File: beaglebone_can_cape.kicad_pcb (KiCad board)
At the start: 2 copper layers, 86.4 x 54.6 mm, 28 parts, among them J1 DCAN0, J2 DCAN1, J4 Conn_02x02_Top_Bottom, J5 Battery Harness, P8 BeagleBone_Black_Header, P9 BeagleBone_Black_Header, SW1 SW_Push, U1 TCAN332, U2 TCAN332, U3 LMR51430

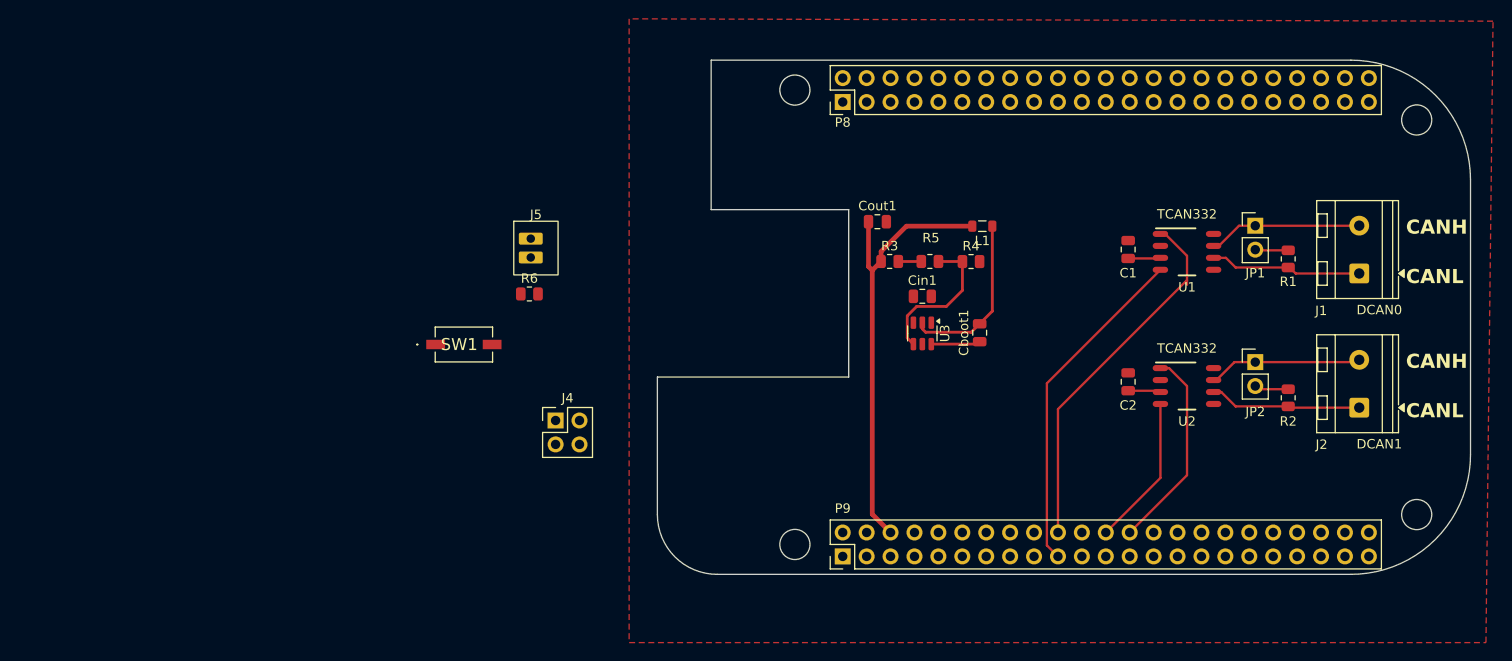
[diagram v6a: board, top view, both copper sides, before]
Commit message: PCB Version 1: Before Week 4 Meeting
* Reorganized the board to support Deutsch
* Assigned all components to have footprints
* Simplified the schematic, namely the pins
* Created the battery circuit and put on PCB

Co-Authored-By: Zach Weidner <119375087+WeidnerZ@users.noreply.github.com>
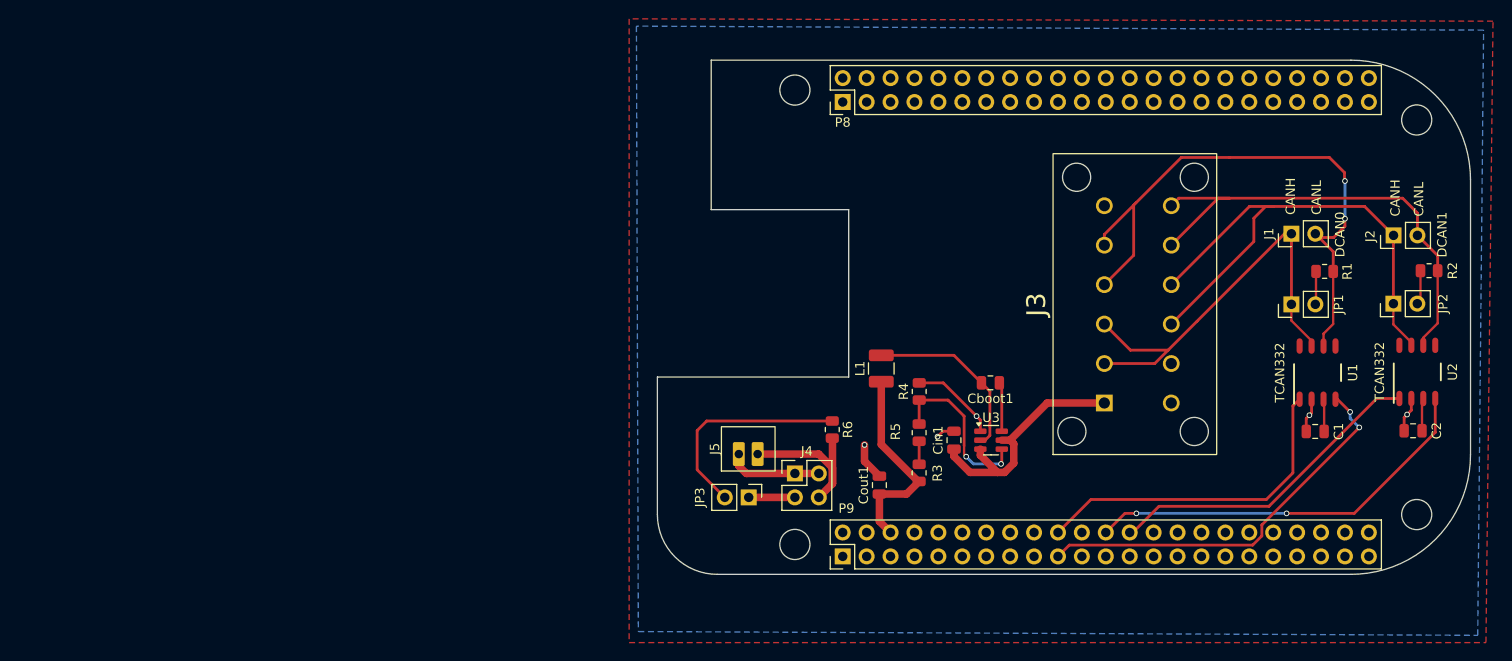
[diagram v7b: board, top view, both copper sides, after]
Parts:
- removed SW1: SW_Push, SeniorDesign:SKQYAAE010
- added J3: DTM15-12PA, Senior Design:TE_DTM15-12PA, F.Cu at (151.0, 71.3)
- added JP3: Jumper_2_Open, Connector_PinHeader_2.54mm:PinHeader_1x02_P2.54mm_Vertical, F.Cu at (109.7, 91.8)
- J1: value DCAN0 -> Conn_01x02_Pin; footprint TerminalBlock_RND:TerminalBlock_RND_205-00232_1x02_P5.08mm_Horizontal -> Connector_PinHeader_2.54mm:PinHeader_1x02_P2.54mm_Vertical
- J2: value DCAN1 -> Conn_01x02_Pin; footprint TerminalBlock_RND:TerminalBlock_RND_205-00232_1x02_P5.08mm_Horizontal -> Connector_PinHeader_2.54mm:PinHeader_1x02_P2.54mm_Vertical
- J5: footprint SeniorDesign:BatteryHolder -> Senior Design:BatteryHolder
- L1: footprint Inductor_SMD:L_0805_2012Metric -> Inductor_SMD:L_1210_3225Metric
- moved R6 35.2 mm to (118.6, 84.6), turned to -90 degrees
- moved J5 31.0 mm to (109.7, 86.7), turned to 90 degrees
- moved C2 30.7 mm to (180.3, 84.8), turned to 180 degrees
- moved Cout1 28.0 mm to (123.6, 90.5), turned to 90 degrees
- moved C1 27.7 mm to (169.9, 84.8), turned to 180 degrees
- moved J4 26.0 mm to (114.6, 89.3)
- moved U2 24.5 mm to (180.7, 78.5), turned to 90 degrees
- moved R3 22.7 mm to (127.8, 89.2), turned to 90 degrees
- moved R2 20.2 mm to (182.0, 67.8), turned to 0 degrees
- moved U1 18.9 mm to (170.1, 78.6), turned to 90 degrees
- moved J2 18.7 mm to (178.2, 64.0)
- moved L1 18.5 mm to (123.8, 78.1), turned to -90 degrees
- moved R5 18.2 mm to (127.8, 85.0), turned to 90 degrees
- moved JP2 15.9 mm to (178.2, 71.2), turned to 90 degrees
- moved Cin1 15.6 mm to (131.5, 85.8), turned to 90 degrees
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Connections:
- Cout1 pad 1: PWR -> +5V
- J1 pad 1: Net-(J1-Pin_1) -> CAN HIGH 0
- J1 pad 2: Net-(J1-Pin_2) -> CAN LOW 0
- J2 pad 1: CAN LOW 1 -> CAN HIGH 1
- J2 pad 2: CAN HIGH 1 -> CAN LOW 1
- JP1 pad 1: Net-(J1-Pin_2) -> CAN HIGH 0
- L1 pad 2: PWR -> +5V
- P8 pad 1: GNDD -> unconnected-(P8-Pin_1-Pad1)
- P8 pad 10: /GPIO68 -> unconnected-(P8-Pin_10-Pad10)
- P8 pad 11: /GPIO45 -> unconnected-(P8-Pin_11-Pad11)
- P8 pad 12: /GPIO44 -> unconnected-(P8-Pin_12-Pad12)
- P8 pad 13: /GPIO23 -> unconnected-(P8-Pin_13-Pad13)
- P8 pad 14: /GPIO26 -> unconnected-(P8-Pin_14-Pad14)
- P8 pad 15: /GPIO47 -> unconnected-(P8-Pin_15-Pad15)
- P8 pad 16: /GPIO46 -> unconnected-(P8-Pin_16-Pad16)
- P8 pad 17: /GPIO27 -> unconnected-(P8-Pin_17-Pad17)
- P8 pad 18: /GPIO65 -> unconnected-(P8-Pin_18-Pad18)
- P8 pad 19: /GPIO22 -> unconnected-(P8-Pin_19-Pad19)
- P8 pad 2: GNDD -> unconnected-(P8-Pin_2-Pad2)
- P8 pad 20: /MMC1.CMD -> unconnected-(P8-Pin_20-Pad20)
- P8 pad 21: /MMC1.CLK -> unconnected-(P8-Pin_21-Pad21)
- P8 pad 22: /MMC1.DAT5 -> unconnected-(P8-Pin_22-Pad22)
- P8 pad 23: /MMC1.DAT4 -> unconnected-(P8-Pin_23-Pad23)
- P8 pad 24: /MMC1.DAT1 -> unconnected-(P8-Pin_24-Pad24)
- P8 pad 25: /MMC1.DAT0 -> unconnected-(P8-Pin_25-Pad25)
- P8 pad 26: /LCD.PCLK -> unconnected-(P8-Pin_26-Pad26)
- P8 pad 27: /LCD.VSYNC -> unconnected-(P8-Pin_27-Pad27)
- P8 pad 28: /GPIO61 -> unconnected-(P8-Pin_28-Pad28)
- P8 pad 29: /LCD.HSYNC -> unconnected-(P8-Pin_29-Pad29)
- P8 pad 3: /MMC1.DAT6 -> unconnected-(P8-Pin_3-Pad3)
- P8 pad 30: /LCD.AC_BIAS_E -> unconnected-(P8-Pin_30-Pad30)
- P8 pad 31: /LCD.DATA14 -> unconnected-(P8-Pin_31-Pad31)
- P8 pad 32: /LCD.DATA15 -> unconnected-(P8-Pin_32-Pad32)
- P8 pad 33: /LCD.DATA13 -> unconnected-(P8-Pin_33-Pad33)
- P8 pad 34: /LCD.DATA11 -> unconnected-(P8-Pin_34-Pad34)
- P8 pad 35: /LCD.DATA12 -> unconnected-(P8-Pin_35-Pad35)
- P8 pad 36: /LCD.DATA10 -> unconnected-(P8-Pin_36-Pad36)
- P8 pad 37: /LCD.DATA8 -> unconnected-(P8-Pin_37-Pad37)
- P8 pad 38: /LCD.DATA9 -> unconnected-(P8-Pin_38-Pad38)
- P8 pad 39: /LCD.DATA6 -> unconnected-(P8-Pin_39-Pad39)
- P8 pad 4: /MMC1.DAT7 -> unconnected-(P8-Pin_4-Pad4)
- P8 pad 40: /LCD.DATA7 -> unconnected-(P8-Pin_40-Pad40)
- P8 pad 41: /LCD.DATA4 -> unconnected-(P8-Pin_41-Pad41)
- P8 pad 42: /LCD.DATA5 -> unconnected-(P8-Pin_42-Pad42)
- P8 pad 43: /LCD.DATA2 -> unconnected-(P8-Pin_43-Pad43)
- P8 pad 44: /LCD.DATA3 -> unconnected-(P8-Pin_44-Pad44)
- P8 pad 45: /LCD.DATA0 -> unconnected-(P8-Pin_45-Pad45)
- P8 pad 46: /LCD.DATA1 -> unconnected-(P8-Pin_46-Pad46)
- P8 pad 5: /MMC1.DAT2 -> unconnected-(P8-Pin_5-Pad5)
- P8 pad 6: /MMC1.DAT3 -> unconnected-(P8-Pin_6-Pad6)
- P8 pad 7: /GPIO66 -> unconnected-(P8-Pin_7-Pad7)
- P8 pad 8: /GPIO67 -> unconnected-(P8-Pin_8-Pad8)
- P8 pad 9: /GPIO69 -> unconnected-(P8-Pin_9-Pad9)
- P9 pad 1: GNDD -> unconnected-(P9-Pin_1-Pad1)
- P9 pad 10: /~{SYS_RESET} -> unconnected-(P9-Pin_10-Pad10)
- P9 pad 11: /GPIO30 -> unconnected-(P9-Pin_11-Pad11)
- P9 pad 12: /GPIO60 -> unconnected-(P9-Pin_12-Pad12)
- P9 pad 13: /GPIO31 -> unconnected-(P9-Pin_13-Pad13)
- P9 pad 14: /GPIO40 -> unconnected-(P9-Pin_14-Pad14)
- P9 pad 15: /GPIO48 -> unconnected-(P9-Pin_15-Pad15)
- P9 pad 16: /GPIO51 -> unconnected-(P9-Pin_16-Pad16)
- P9 pad 17: /GPIO4 -> unconnected-(P9-Pin_17-Pad17)
- P9 pad 18: /GPIO5 -> unconnected-(P9-Pin_18-Pad18)
- P9 pad 2: GNDD -> unconnected-(P9-Pin_2-Pad2)
- P9 pad 21: /GPIO3 -> unconnected-(P9-Pin_21-Pad21)
- P9 pad 22: /GPIO2 -> unconnected-(P9-Pin_22-Pad22)
- P9 pad 23: /GPIO49 -> unconnected-(P9-Pin_23-Pad23)
- P9 pad 25: /GPIO117 -> unconnected-(P9-Pin_25-Pad25)
- P9 pad 27: /GPIO125 -> unconnected-(P9-Pin_27-Pad27)
- P9 pad 28: /SPI1.CS0 -> unconnected-(P9-Pin_28-Pad28)
- P9 pad 29: /SPI1.D0 -> unconnected-(P9-Pin_29-Pad29)
- P9 pad 3: +3V3 -> unconnected-(P9-Pin_3-Pad3)
- P9 pad 30: /GPIO122 -> unconnected-(P9-Pin_30-Pad30)
- P9 pad 31: /SPI1.SCLK -> unconnected-(P9-Pin_31-Pad31)
- P9 pad 32: +1V8 -> unconnected-(P9-Pin_32-Pad32)
- P9 pad 33: /AIN4 -> unconnected-(P9-Pin_33-Pad33)
- P9 pad 34: GNDA -> unconnected-(P9-Pin_34-Pad34)
- P9 pad 35: /AIN6 -> unconnected-(P9-Pin_35-Pad35)
- P9 pad 36: /AIN5 -> unconnected-(P9-Pin_36-Pad36)
- P9 pad 37: /AIN2 -> unconnected-(P9-Pin_37-Pad37)
- P9 pad 38: /AIN3 -> unconnected-(P9-Pin_38-Pad38)
- P9 pad 39: /AIN0 -> unconnected-(P9-Pin_39-Pad39)
- P9 pad 4: +3V3 -> unconnected-(P9-Pin_4-Pad4)
- P9 pad 40: /AIN1 -> unconnected-(P9-Pin_40-Pad40)
- P9 pad 41: /GPIO20 -> unconnected-(P9-Pin_41-Pad41)
- P9 pad 42: /GPIO7 -> unconnected-(P9-Pin_42-Pad42)
- P9 pad 43: GNDD -> unconnected-(P9-Pin_43-Pad43)
- P9 pad 44: GNDD -> unconnected-(P9-Pin_44-Pad44)
- P9 pad 45: GNDD -> unconnected-(P9-Pin_45-Pad45)
- P9 pad 46: GNDD -> unconnected-(P9-Pin_46-Pad46)
- P9 pad 5: PWR -> unconnected-(P9-Pin_5-Pad5)
- P9 pad 7: VBUS -> unconnected-(P9-Pin_7-Pad7)
- P9 pad 8: VBUS -> unconnected-(P9-Pin_8-Pad8)
- P9 pad 9: /PWR_BUT -> unconnected-(P9-Pin_9-Pad9)
- R1 pad 2: Net-(J1-Pin_1) -> CAN LOW 0
- R3 pad 1: PWR -> +5V
- U1 pad 6: Net-(J1-Pin_1) -> CAN LOW 0
- U1 pad 7: Net-(J1-Pin_2) -> CAN HIGH 0
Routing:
- net CAN LOW 0: track 0.00 -> 63.1 mm, vias 0 -> 2
- net CAN HIGH 0: track 0.00 -> 46.3 mm
- net CAN HIGH 1: track 16.4 -> 58.3 mm
- net CAN LOW 1: track 16.2 -> 50.9 mm
- net /GPIO15: track 16.1 -> 43.0 mm, vias 0 -> 2
- net +24V: track 0.00 -> 26.6 mm
- net +5V: track 47.2 -> 21.7 mm
- net Net-(JP3-B): track 0.00 -> 23.1 mm
- net GND: track 0.00 -> 22.7 mm, vias 0 -> 5
- net Net-(J4-Pin_4): track 0.00 -> 17.1 mm
- net Net-(J1-Pin_2): track 16.4 -> 0.00 mm
- net Net-(J1-Pin_1): track 16.2 -> 0.00 mm
- net /GPIO14: track 21.7 -> 34.5 mm
- net Net-(J4-Pin_1): track 0.00 -> 10.1 mm
- net /I2C2.SCL: track 35.9 -> 42.5 mm, vias 0 -> 2
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- added copper zone on B.Cu, net GND

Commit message: pushing for nash work
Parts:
- added D1: CUHZ36V, SeniorDesign:TVSDiode, F.Cu at (131.7, 91.2)
- J3: footprint Senior Design:TE_DTM15-12PA -> SeniorDesign:Deutsch_Marlin
- J5: footprint Senior Design:BatteryHolder -> SeniorDesign:BatteryHolder
- moved J3 1.51 mm to (151.0, 72.8)
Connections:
- P8 pad 1: unconnected-(P8-Pin_1-Pad1) -> GNDD
- P8 pad 2: unconnected-(P8-Pin_2-Pad2) -> GNDD
- P9 pad 1: unconnected-(P9-Pin_1-Pad1) -> GNDD
- P9 pad 2: unconnected-(P9-Pin_2-Pad2) -> GNDD
- P9 pad 3: unconnected-(P9-Pin_3-Pad3) -> +3V3
- P9 pad 4: unconnected-(P9-Pin_4-Pad4) -> +3V3
- P9 pad 43: unconnected-(P9-Pin_43-Pad43) -> GNDD
- P9 pad 44: unconnected-(P9-Pin_44-Pad44) -> GNDD
- P9 pad 45: unconnected-(P9-Pin_45-Pad45) -> GNDD
- P9 pad 46: unconnected-(P9-Pin_46-Pad46) -> GNDD
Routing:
- net CAN HIGH 1: track 58.3 -> 12.5 mm
- net CAN LOW 0: track 63.1 -> 21.7 mm
- net CAN LOW 1: track 50.9 -> 13.2 mm
- net CAN HIGH 0: track 46.3 -> 12.8 mm
- net +24V: track 26.6 -> 17.4 mm
- net GND: track 22.7 -> 24.4 mm, vias 5 -> 6
